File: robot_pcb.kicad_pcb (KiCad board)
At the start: 4 copper layers, 140 x 180 mm, 192 parts, among them J1 Raspberry_Pi_2_3, J10 Servo_TrayRelease, J14 Motor FR, J17 Programmer, J18 USB_C_Receptacle_PowerOnly_6P, J2 Power_Bypass, J23 Motor BR, J25 ConductClaw, J26 Motor BL, J27 TOF_Front, J28 OLED_Display, J29 Motor FL, J3 Lipo, J4 TOF_Right, J5 TOF_Back, J6 TOF_Claw, J7 UltraS_Side, J8 Servo_Grab, J9 Servo_Lift, Q2 Q_NMOS_GDS, SW1 SW_SPDT, SW2 SW_Push, U1 STM32F407VGTx, U10 DMG2305UX-7, U11 DMG2305UX-7, U2 BQ76920PW, U3 AP64501SP-13, U4 MAX25240AFFD/VY+, U5 DMG2305UX-7, U6 AP64501SP-13, U7 AP64501SP-13, U9 BNO086, Y1 25MHz, Y2 32.768kHz

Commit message: bro why did it do that i thought i fixed that anyway its fixed now
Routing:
- net /TIM2_CH1: track 111.4 -> 96.7 mm
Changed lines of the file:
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@@
 	)
 	(segment
-		(start 89.701 197.665083)
-		(end 90.056083 197.31)
+		(start 92.575 191.60637)
+		(end 89.75 188.78137)
 		(width 0.3)
 		(layer "F.Cu")
@@
 	)
 	(segment
-		(start 91.951 195.867083)
-		(end 91.951 196.654917)
+		(start 96.05 113.236)
+		(end 93.65 113.236)
 		(width 0.3)
 		(layer "F.Cu")
@@
 	)
 	(segment
-		(start 87.475 193.54163)
-		(end 87.59413 193.4225)
+		(start 89.75 188.78137)
+		(end 89.75 136.086)
+		(width 0.3)
+		(layer "F.Cu")
+		(net 108)
+	)
+	(segment
+		(start 89.75 136.086)
+		(end 96.926 128.91)
+		(width 0.3)
+		(layer "F.Cu")
+		(net 108)
+	)
+	(segment
+		(start 92.575 200.411)
+		(end 92.575 191.60637)
+		(width 0.3)
+		(layer "F.Cu")
+		(net 108)
+	)
+	(segment
+		(start 96.926 128.91)
+		(end 96.926 114.112)
+		(width 0.3)
+		(layer "F.Cu")
+		(net 108)
+	)
+	(segment
+		(start 90.725 202.261)
+		(end 92.575 200.411)
 		(width 0.3)
 		(layer "F.Cu")
@@
 	(segment
 		(start 96.926 114.112)
-		(end 96.926 128.91)
-		(width 0.3)
-		(layer "F.Cu")
-		(net 108)
-	)
-	(segment
-		(start 89.701 196.856917)
-		(end 89.701 197.665083)
-		(width 0.3)
-		(layer "F.Cu")
-		(net 108)
-	)
-	(segment
-		(start 89.499 199.867083)
-		(end 89.499 200.654917)
-		(width 0.3)
-		(layer "F.Cu")
-		(net 108)
-	)
-	(segment
-		(start 89.606083 198.762)
-		(end 89.33252 198.762)
-		(width 0.3)
-		(layer "F.Cu")
-		(net 108)
-	)
-	(segment
-		(start 96.05 113.236)
-		(end 96.926 114.112)
-		(width 0.3)
-		(layer "F.Cu")
-		(net 108)
-	)
-	(segment
-		(start 87.475 138.361)
-		(end 87.475 193.54163)
-		(width 0.3)
-		(layer "F.Cu")
-		(net 108)
-	)
-	(segment
-		(start 89.35587 193.4225)
-		(end 89.701 193.76763)
-		(width 0.3)
-		(layer "F.Cu")
-		(net 108)
-	)
-	(segment
-		(start 91.326 201.212)
-		(end 92.375 202.261)
-		(width 0.3)
-		(layer "F.Cu")
-		(net 108)
-	)
-	(segment
-		(start 91.951 197.867083)
-		(end 91.951 198.654917)
-		(width 0.3)
-		(layer "F.Cu")
-		(net 108)
-	)
-	(segment
-		(start 92.375 202.261)
-		(end 90.725 202.261)
-		(width 0.3)
-		(layer "F.Cu")
-		(net 108)
-	)
-	(segment
-		(start 91.393917 197.31)
-		(end 91.951 197.867083)
-		(width 0.3)
-		(layer "F.Cu")
-		(net 108)
-	)
-	(segment
-		(start 89.499 200.654917)
-		(end 90.056083 201.212)
-		(width 0.3)
-		(layer "F.Cu")
-		(net 108)
-	)
-	(segment
-		(start 87.59413 193.4225)
-		(end 89.35587 193.4225)
-		(width 0.3)
-		(layer "F.Cu")
-		(net 108)
-	)
-	(segment
-		(start 91.951 196.654917)
-		(end 91.393917 197.212)
-		(width 0.3)
-		(layer "F.Cu")
-		(net 108)
-	)
-	(segment
-		(start 96.926 128.91)
-		(end 87.475 138.361)
-		(width 0.3)
-		(layer "F.Cu")
-		(net 108)
-	)
-	(segment
-		(start 89.33252 198.762)
-		(end 89.10426 198.99026)
-		(width 0.3)
-		(layer "F.Cu")
-		(net 108)
-	)
-	(segment
-		(start 90.056083 197.31)
-		(end 91.393917 197.31)
-		(width 0.3)
-		(layer "F.Cu")
-		(net 108)
-	)
-	(segment
-		(start 90.056083 199.212)
-		(end 89.606083 198.762)
-		(width 0.3)
-		(layer "F.Cu")
-		(net 108)
-	)
-	(segment
-		(start 90.48252 195.31)
-		(end 91.393917 195.31)
-		(width 0.3)
-		(layer "F.Cu")
-		(net 108)
-	)
-	(segment
-		(start 91.393917 197.212)
-		(end 90.056083 197.212)
-		(width 0.3)
-		(layer "F.Cu")
-		(net 108)
-	)
-	(segment
-		(start 90.04902 194.8765)
-		(end 90.48252 195.31)
-		(width 0.3)
-		(layer "F.Cu")
-		(net 108)
-	)
-	(segment
-		(start 89.701 193.76763)
-		(end 89.701 194.8765)
-		(width 0.3)
-		(layer "F.Cu")
-		(net 108)
-	)
-	(segment
-		(start 93.65 113.236)
 		(end 96.05 113.236)
 		(width 0.3)
 		(layer "F.Cu")
-		(net 108)
-	)
-	(segment
-		(start 89.740042 199.626042)
-		(end 89.499 199.867083)
-		(width 0.3)
-		(layer "F.Cu")
-		(net 108)
-	)
-	(segment
-		(start 89.701 194.8765)
-		(end 90.04902 194.8765)
-		(width 0.3)
-		(layer "F.Cu")
-		(net 108)
-	)
-	(segment
-		(start 91.393917 195.31)
-		(end 91.951 195.867083)
-		(width 0.3)
-		(layer "F.Cu")
-		(net 108)
-	)
-	(segment
-		(start 90.056083 197.212)
-		(end 89.701 196.856917)
-		(width 0.3)
-		(layer "F.Cu")
-		(net 108)
-	)
-	(segment
-		(start 89.10426 198.99026)
-		(end 89.740042 199.626042)
-		(width 0.3)
-		(layer "F.Cu")
-		(net 108)
-	)
-	(segment
-		(start 91.393917 199.212)
-		(end 90.056083 199.212)
-		(width 0.3)
-		(layer "F.Cu")
-		(net 108)
-	)
-	(segment
-		(start 90.056083 201.212)
-		(end 91.326 201.212)
-		(width 0.3)
-		(layer "F.Cu")
-		(net 108)
-	)
-	(segment
-		(start 91.951 198.654917)
-		(end 91.393917 199.212)
-		(width 0.3)
-		(layer "F.Cu")

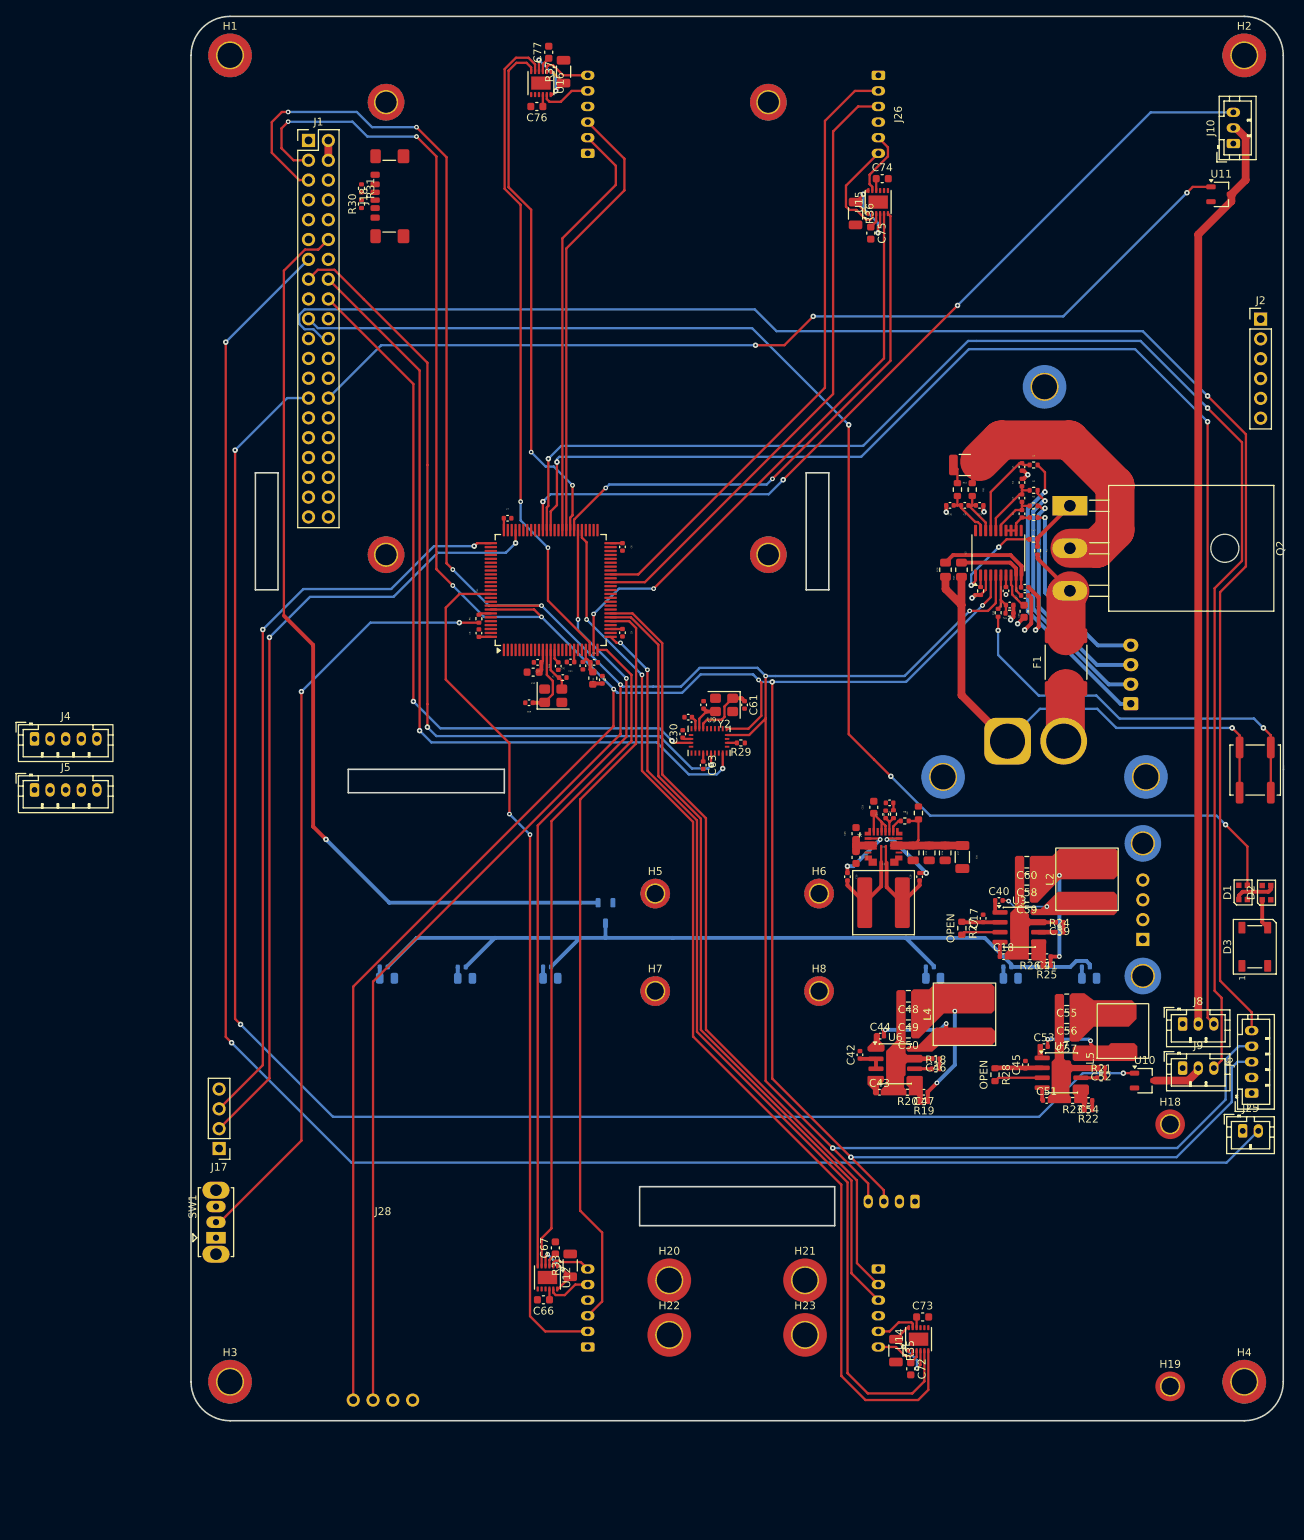
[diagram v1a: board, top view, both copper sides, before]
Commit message: Shifted whole pcb + connected tofs
Hopefully pcb is aligned to the grid now. Somebody please check my wiring bc it's probably cooked but I gave it a go anyway.
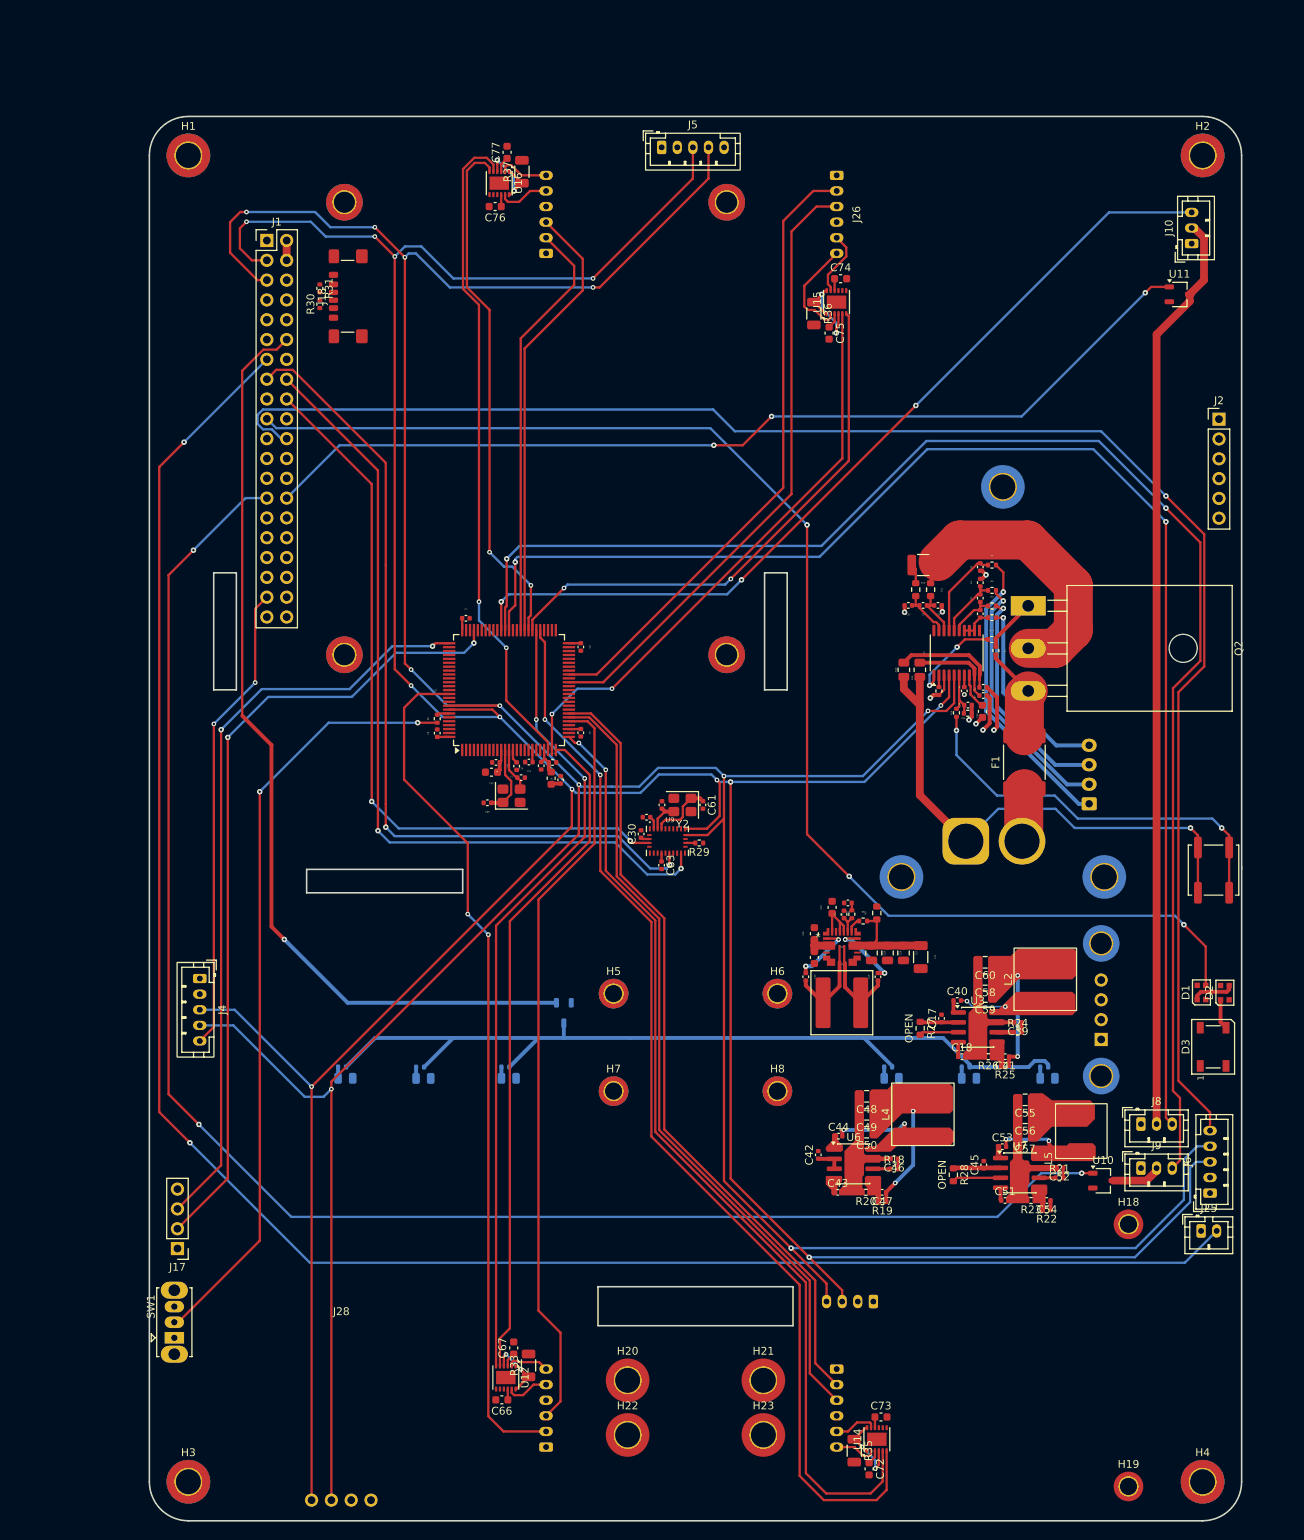
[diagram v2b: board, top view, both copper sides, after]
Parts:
- moved J5 115.1 mm to (100.2, 52.5)
- moved J4 37.3 mm to (41.0, 159.0), turned to -90 degrees
- moved H5 13.9 mm to (94.0, 161.0)
- moved C61 13.9 mm to (105.5, 136.8)
- moved C62 13.9 mm to (100.2, 136.8)
- moved C70 13.9 mm to (82.2, 133.3)
- moved Y2 13.9 mm to (102.9, 136.8)
- moved C11 13.9 mm to (83.2, 131.3)
- moved C15 13.9 mm to (87.3, 133.6)
- moved C75 13.9 mm to (121.7, 76.3)
- moved J1 13.9 mm to (49.6, 64.4)
- moved R31 13.9 mm to (56.4, 70.6)
- moved C18 13.9 mm to (138.7, 169.1)
- moved C26 13.9 mm to (129.1, 155.8)
- moved C31 13.9 mm to (133.4, 156.3)
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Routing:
- net /I2C_SCL: track 425.4 -> 497.1 mm, vias 8 -> 11
- net /I2C_SDA: track 421.2 -> 489.3 mm, vias 9 -> 12
- net /GPIO26: track 0.00 -> 60.4 mm, vias 0 -> 2
- net Net-(J1-GPIO27): track 244.8 -> 247.4 mm
- net /GPIO0: track 207.9 -> 210.5 mm
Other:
- outline, holes or cut-outs redrawn
- board text removed: "${REFERENCE}"

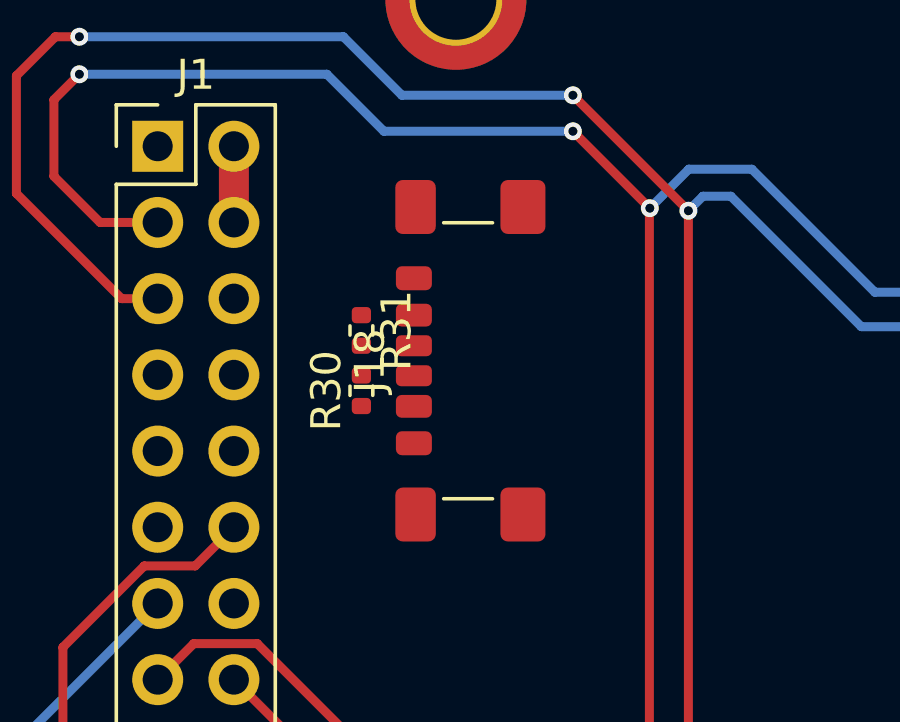
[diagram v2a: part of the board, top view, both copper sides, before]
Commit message: changed usb connector footprint
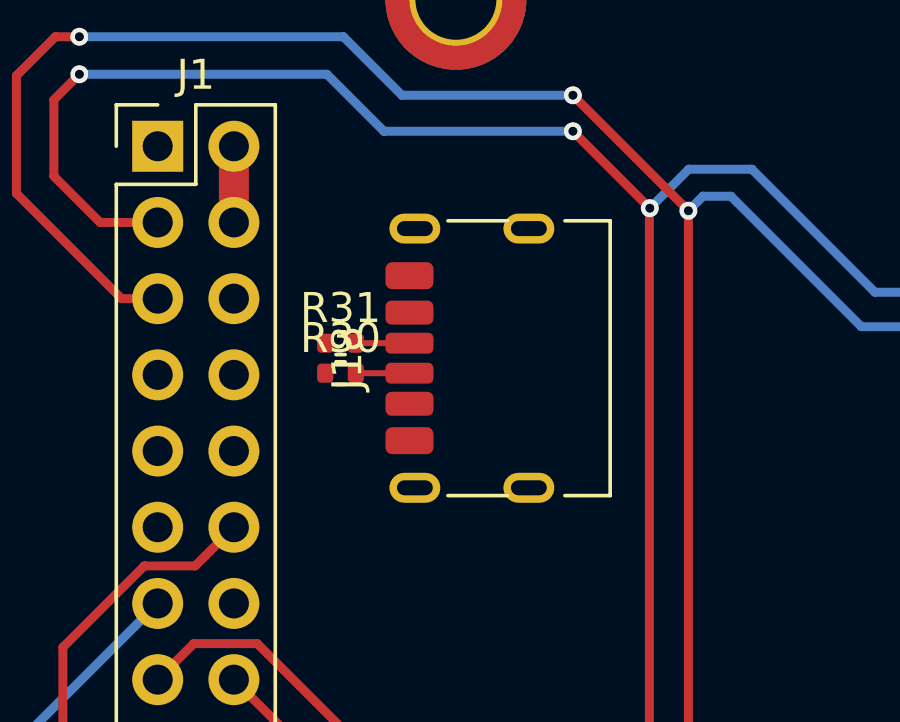
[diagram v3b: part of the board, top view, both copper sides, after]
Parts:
- J18: footprint Connector_USB:USB_C_Receptacle_GCT_USB4135-GF-A_6P_TopMnt_Horizontal -> Connector_USB:USB_C_Receptacle_HRO_TYPE-C-31-M-17
- moved R30 0.91 mm to (55.7, 72.0), turned to 0 degrees
- moved R31 0.81 mm to (55.7, 71.0), turned to 0 degrees
- moved J18 0.09 mm to (61.2, 71.5)
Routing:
- net /CC2: track 0.00 -> 1.79 mm
- net /CC1: track 0.00 -> 1.79 mm

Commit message: jetson holes
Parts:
- added H24: MountingHole, MountingHole:MountingHole_2.7mm_M2.5_DIN965_Pad_TopBottom, F.Cu at (54.5, 53.5)
- added H25: MountingHole, MountingHole:MountingHole_2.7mm_M2.5_DIN965_Pad_TopBottom, F.Cu at (112.5, 53.5)
- added H26: MountingHole, MountingHole:MountingHole_2.7mm_M2.5_DIN965_Pad_TopBottom, F.Cu at (54.5, 139.5)
- added H27: MountingHole, MountingHole:MountingHole_2.7mm_M2.5_DIN965_Pad_TopBottom, F.Cu at (112.5, 139.5)
- moved J5 1.83 mm to (98.4, 52.4)
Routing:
- net /I2C_SDA: track 489.3 -> 488.7 mm
- net /I2C_SCL: track 497.1 -> 496.5 mm
